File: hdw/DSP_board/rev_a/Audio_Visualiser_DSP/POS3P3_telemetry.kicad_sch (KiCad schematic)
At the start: 0 parts

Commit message: Added POS3P3 telemetry
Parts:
- added C501, C502, C503: 0.1uF, Capacitors_SMD:C_0402, symbol Custom_Library:C_Custom
- added DOC501, DOC502: TBD, symbol Custom_Library:I2C_Address
- added U501: INA231A, Custom Footprints Library:Texas_DSBGA-12_1.65x1.39mm_Layout3x4_P0.4mm, symbol Custom Library:INA231A
- added U502: MCP9804, Package_DFN_QFN:DFN-8-1EP_3x2mm_P0.5mm_EP1.3x1.5mm, symbol Sensor_Temperature:MCP9804_DFN
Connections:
- new net +3.3V: C502.1, C503.1, U501.B1 (VS), U501.D1 (BUS), U502.8 (V_{DD})
- new net GND: C502.2, C503.2, U501.C1 (GND), U502.4 (GND), U502.9 (EP/GND)
- new net I2C_SCL: U501.A1 (SCL), U502.2 (SCL)
- new net I2C_SDA: U501.A2 (SDA), U502.1 (SDA)
- new net POS3P3_SNS+: C501.1, U501.D3 (IN+)
- new net POS3P3_SNS-: C501.2, U501.D2 (IN-)
- no-connect marks 0 -> 2
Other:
- note added: "Max Current = 3.1A RSHUNT = 0.02 Ohm CLSB = 9.46045E-05A CAL Register = 0x0A92"

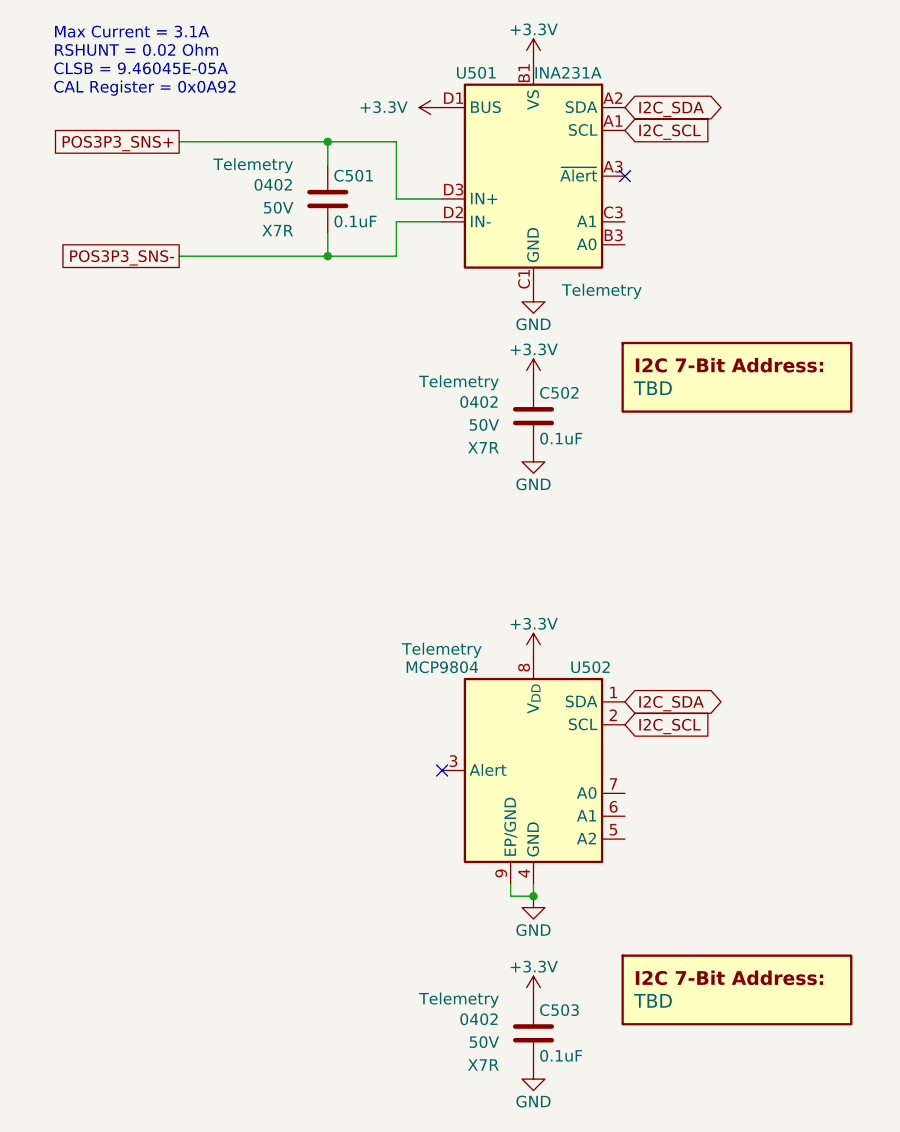
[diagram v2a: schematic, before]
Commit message: Defined legit KiCad BOM variants
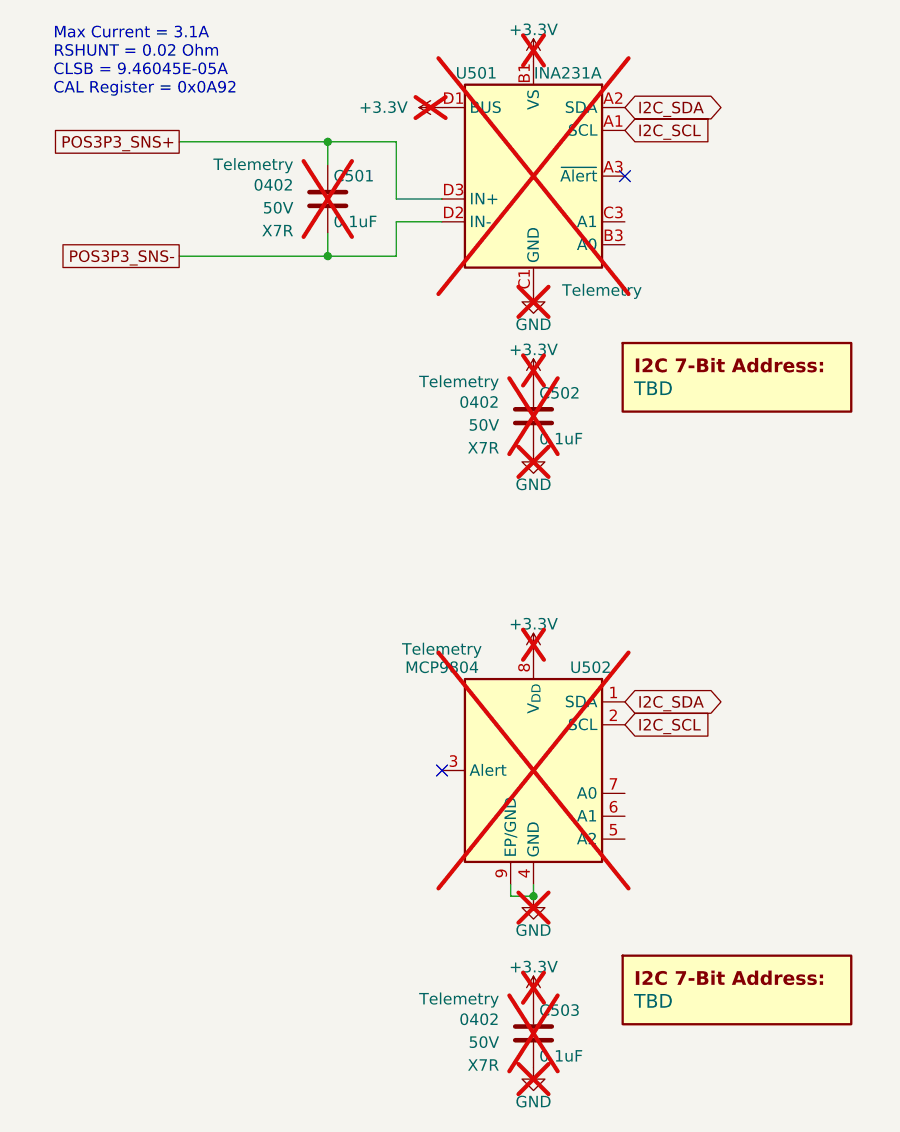
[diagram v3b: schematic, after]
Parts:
- C501, C502, C503, U501, U502: now not fitted
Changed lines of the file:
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@@
 		(on_board yes)
 		(in_pos_files yes)
-		(dnp no)
+		(dnp yes)
 		(property "Reference" "#PWR0508"
 			(at 132.08 148.59 0)
@@
 		(on_board yes)
 		(in_pos_files yes)
-		(dnp no)
+		(dnp yes)
 		(property "Reference" "#PWR0506"
 			(at 132.08 110.49 0)
@@
 		(on_board yes)
 		(in_pos_files yes)
-		(dnp no)
+		(dnp yes)
 		(property "Reference" "U501"
 			(at 125.73 41.91 0)
@@
 					(reference "U501")
 					(unit 1)
+					(variant
+						(name "Default")
+					)
+					(variant
+						(name "Development")
+						(dnp no)
+					)
 				)
 			)
@@
 		(on_board yes)
 		(in_pos_files yes)
-		(dnp no)
+		(dnp yes)
 		(fields_autoplaced yes)
 		(property "Reference" "#PWR0501"
@@
 					(reference "DOC501")
 					(unit 1)
+					(variant
+						(name "Default")
+					)
+					(variant
+						(name "Development")
+					)
 				)
 			)
@@
 		(on_board yes)
 		(in_pos_files yes)
-		(dnp no)
+		(dnp yes)
 		(property "Reference" "#PWR0503"
 			(at 132.08 72.39 0)
@@
 		(on_board yes)
 		(in_pos_files yes)
-		(dnp no)
+		(dnp yes)
 		(property "Reference" "#PWR0502"
 			(at 132.08 44.45 0)
@@
 					(reference "DOC502")
 					(unit 1)
+					(variant
+						(name "Default")
+					)
+					(variant
+						(name "Development")
+					)
 				)
 			)
@@
 		(on_board yes)
 		(in_pos_files yes)
-		(dnp no)
+		(dnp yes)
 		(property "Reference" "#PWR0505"
 			(at 132.08 90.17 0)
@@
 		(on_board yes)
 		(in_pos_files yes)
-		(dnp no)
+		(dnp yes)
 		(property "Reference" "C502"
 			(at 132.715 77.47 0)
@@
 					(reference "C502")
 					(unit 1)
+					(variant
+						(name "Default")
+					)
+					(variant
+						(name "Development")
+						(dnp no)
+					)
 				)
 			)
@@
 		(on_board yes)
 		(in_pos_files yes)
-		(dnp no)
+		(dnp yes)
 		(property "Reference" "C503"
 			(at 132.715 146.05 0)
@@
 					(reference "C503")
 					(unit 1)
+					(variant
+						(name "Default")
+					)
+					(variant
+						(name "Development")
+						(dnp no)
+					)
 				)
 			)
@@
 		(on_board yes)
 		(in_pos_files yes)
-		(dnp no)
+		(dnp yes)
 		(property "Reference" "#PWR0509"
 			(at 132.08 158.75 0)
@@
 		(on_board yes)
 		(in_pos_files yes)
-		(dnp no)
+		(dnp yes)
 		(property "Reference" "#PWR0504"
 			(at 132.08 80.01 0)
@@
 		(on_board yes)
 		(in_pos_files yes)
-		(dnp no)
+		(dnp yes)
 		(property "Reference" "#PWR0507"
 			(at 132.08 139.7 0)
@@
 		(on_board yes)
 		(in_pos_files yes)
-		(dnp no)
+		(dnp yes)
 		(property "Reference" "U502"
 			(at 138.43 107.95 0)
@@
 					(reference "U502")
 					(unit 1)
+					(variant
+						(name "Default")
+					)
+					(variant
+						(name "Development")
+						(dnp no)
+					)
 				)
 			)
@@
 		(on_board yes)
 		(in_pos_files yes)
-		(dnp no)
+		(dnp yes)
 		(property "Reference" "C501"
 			(at 109.855 53.34 0)
@@
 					(reference "C501")
 					(unit 1)
-				)
-			)
+					(variant
+						(name "Default")
+					)
+					(variant
+						(name "Development")
+						(dnp no)
+					)
+				)
+			)

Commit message: set I2C addresses
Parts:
- DOC501: value TBD -> 0x41
- DOC502: value TBD -> 0x19
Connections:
- net +3.3V: now also U501.B3 (A0), U502.7 (A0)
- net GND: now also U501.C3 (A1), U502.5 (A2), U502.6 (A1)

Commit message: Assigned I2C addresses
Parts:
- DOC501: value 0x41 -> 0x43
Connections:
- net +3.3V: no longer U501.B3 (A0)
- net I2C_SCL: now also U501.B3 (A0)
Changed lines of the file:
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@@
+		)
+	)
+	(global_label "I2C_SCL"
+		(shape input)
+		(at 142.24 60.96 0)
+		(fields_autoplaced yes)
+		(effects
+			(font
+				(size 1.27 1.27)
+			)
+			(justify left)
+		)
+		(property "Intersheetrefs" "${INTERSHEET_REFS}"
+			(at 152.7053 60.96 0)
+			(hide yes)
+			(show_name no)
+			(do_not_autoplace no)
+			(effects
+				(font
+					(size 1.27 1.27)
+				)
+				(justify left)
+			)
 		)
 	)
@@
 	)
 	(symbol
+		(lib_name "GND_1")
+		(lib_id "power:GND")
+		(at 142.24 58.42 90)
+		(unit 1)
+		(body_style 1)
+		(exclude_from_sim no)
+		(in_bom yes)
+		(on_board yes)
+		(in_pos_files yes)
+		(dnp no)
+		(fields_autoplaced yes)
+		(property "Reference" "#PWR0510"
+			(at 148.59 58.42 0)
+			(hide yes)
+			(show_name no)
+			(do_not_autoplace no)
+			(effects
+				(font
+					(size 1.27 1.27)
+				)
+			)
+		)
+		(property "Value" "GND"
+			(at 146.05 58.4199 90)
+			(show_name no)
+			(do_not_autoplace no)
+			(effects
+				(font
+					(size 1.27 1.27)
+				)
+				(justify right)
+			)
+		)
+		(property "Footprint" ""
+			(at 142.24 58.42 0)
+			(hide yes)
+			(show_name no)
+			(do_not_autoplace no)
+			(effects
+				(font
+					(size 1.27 1.27)
+				)
+			)
+		)
+		(property "Datasheet" ""
+			(at 142.24 58.42 0)
+			(hide yes)
+			(show_name no)
+			(do_not_autoplace no)
+			(effects
+				(font
+					(size 1.27 1.27)
+				)
+			)
+		)
+		(property "Description" "Power symbol creates a global label with name \"GND\" , ground"
+			(at 142.24 58.42 0)
+			(hide yes)
+			(show_name no)
+			(do_not_autoplace no)
+			(effects
+				(font
+					(size 1.27 1.27)
+				)
+			)
+		)
+		(pin "1"
+		)
+		(instances
+			(project "Audio_Visualiser_DSP"
+				(path "/97a4dfb8-0e16-46f1-9709-8d2007dd0cd3/591fe591-cb36-4c0a-afd1-91c877291a0e"
+					(reference "#PWR0510")
+					(unit 1)
+				)
+			)
+		)
+	)
+	(symbol
 		(lib_id "power:+3.3V")
 		(at 132.08 144.78 0)
@@
 			)
 		)
-		(property "Value" "0x41"
+		(property "Value" "0x43"
 			(at 143.256 76.962 0)
 			(show_name no)
@@
 						(name "Development")
 						(dnp no)
-					)
-				)
-			)
-		)
-	)
-	(symbol
-		(lib_id "power:+3.3V")
-		(at 142.24 60.96 270)
-		(unit 1)
-		(body_style 1)
-		(exclude_from_sim yes)
-		(in_bom yes)
-		(on_board yes)
-		(in_pos_files yes)
-		(dnp no)
-		(fields_autoplaced yes)
-		(property "Reference" "#PWR0514"
-			(at 138.43 60.96 0)
-			(hide yes)
-			(show_name no)
-			(do_not_autoplace no)
-			(effects
-				(font
-					(size 1.27 1.27)
-				)
-			)
-		)
-		(property "Value" "+3.3V"
-			(at 146.05 60.9599 90)
-			(show_name no)
-			(do_not_autoplace no)
-			(effects
-				(font
-					(size 1.27 1.27)
-				)
-				(justify left)
-			)
-		)
-		(property "Footprint" ""
-			(at 142.24 60.96 0)
-			(hide yes)
-			(show_name no)
-			(do_not_autoplace no)
-			(effects
-				(font
-					(size 1.27 1.27)
-				)
-			)
-		)
-		(property "Datasheet" ""
-			(at 142.24 60.96 0)
-			(hide yes)
-			(show_name no)
-			(do_not_autoplace no)
-			(effects
-				(font
-					(size 1.27 1.27)
-				)
-			)
-		)
-		(property "Description" "Power symbol creates a global label with name \"+3.3V\""
-			(at 142.24 60.96 0)
-			(hide yes)
-			(show_name no)
-			(do_not_autoplace no)
-			(effects
-				(font
-					(size 1.27 1.27)
-				)
-			)
-		)
-		(pin "1"
-		)
-		(instances
-			(project "Audio_Visualiser_DSP"
-				(path "/97a4dfb8-0e16-46f1-9709-8d2007dd0cd3/591fe591-cb36-4c0a-afd1-91c877291a0e"
-					(reference "#PWR0514")
-					(unit 1)
-					(variant
-						(name "Development")
 					)
 				)
@@
 					(unit 1)
 				)
-			)
-		)
-	)
-	(symbol
-		(lib_name "GND_1")
-		(lib_id "power:GND")
-		(at 142.24 58.42 90)
-		(unit 1)
-		(body_style 1)
-		(exclude_from_sim no)
-		(in_bom yes)
-		(on_board yes)
-		(in_pos_files yes)
-		(dnp no)
-		(fields_autoplaced yes)
-		(property "Reference" "#PWR0510"
-			(at 148.59 58.42 0)
-			(hide yes)
-			(show_name no)
-			(do_not_autoplace no)
-			(effects
-				(font
-					(size 1.27 1.27)
-				)
-			)
-		)
-		(property "Value" "GND"
-			(at 146.05 58.4199 90)
-			(show_name no)
-			(do_not_autoplace no)
-			(effects
-				(font
-					(size 1.27 1.27)
-				)
-				(justify right)
-			)
-		)
-		(property "Footprint" ""
-			(at 142.24 58.42 0)
-			(hide yes)
-			(show_name no)
-			(do_not_autoplace no)
-			(effects
-				(font
-					(size 1.27 1.27)
-				)
-			)
-		)
-		(property "Datasheet" ""
-			(at 142.24 58.42 0)
-			(hide yes)
-			(show_name no)
-			(do_not_autoplace no)
-			(effects
-				(font
-					(size 1.27 1.27)
-				)
-			)
-		)
-		(property "Description" "Power symbol creates a global label with name \"GND\" , ground"
-			(at 142.24 58.42 0)
-			(hide yes)
-			(show_name no)
-			(do_not_autoplace no)
-			(effects
-				(font
-					(size 1.27 1.27)
-				)
-			)
-		)
-		(pin "1"
-		)
-		(instances
-			(project "Audio_Visualiser_DSP"
-				(path "/97a4dfb8-0e16-46f1-9709-8d2007dd0cd3/591fe591-cb36-4c0a-afd1-91c877291a0e"
-					(reference "#PWR0510")
-					(unit 1)
-				)

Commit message: Consolidated onto a single project library
This commit combines all schematic symbols, pcb footprints, and 3d models into a single project library for portability. Still have a few 3d models to add yet. It also removes each individual custom component which had been stored in this repo earlier
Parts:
- C501, C502, C503: footprint Capacitors_SMD:C_0402 -> project_lib:C_0402; symbol Custom_Library:C_Custom -> project_lib:C_Custom
- DOC501, DOC502: symbol Custom_Library:I2C_Address -> project_lib:I2C_Address
- U501: footprint Custom Footprints Library:Texas_DSBGA-12_1.65x1.39mm_Layout3x4_P0.4mm -> project_lib:Texas_DSBGA-12_1.65x1.39mm_Layout3x4_P0.4mm; symbol Custom Library:INA231A -> project_lib:INA231A
- U502: footprint Package_DFN_QFN:DFN-8-1EP_3x2mm_P0.5mm_EP1.3x1.5mm -> project_lib:DFN-8-1EP_3x2mm_P0.5mm_EP1.3x1.5mm; symbol Sensor_Temperature:MCP9804_DFN -> project_lib:MCP9804_DFN
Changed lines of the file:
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@@
 	)
 	(symbol
-		(lib_name "GND_1")
-		(lib_id "power:GND")
+		(lib_id "project_lib:GND")
 		(at 142.24 58.42 90)
 		(unit 1)
@@
 	)
 	(symbol
-		(lib_id "power:+3.3V")
+		(lib_id "project_lib:+3.3V")
 		(at 132.08 144.78 0)
 		(unit 1)
@@
 	)
 	(symbol
-		(lib_id "power:+3.3V")
+		(lib_id "project_lib:+3.3V")
 		(at 132.08 106.68 0)
 		(unit 1)
@@
 	)
 	(symbol
-		(lib_id "Custom Library:INA231A")
+		(lib_id "project_lib:INA231A")
 		(at 132.08 53.34 0)
 		(unit 1)
@@
 			)
 		)
-		(property "Footprint" "Custom Footprints Library:Texas_DSBGA-12_1.65x1.39mm_Layout3x4_P0.4mm"
+		(property "Footprint" "project_lib:Texas_DSBGA-12_1.65x1.39mm_Layout3x4_P0.4mm"
 			(at 152.4 64.77 0)
 			(hide yes)
@@
 	)
 	(symbol
-		(lib_id "power:+3.3V")
+		(lib_id "project_lib:+3.3V")
 		(at 121.92 45.72 90)
 		(unit 1)
@@
 	)
 	(symbol
-		(lib_id "Custom_Library:I2C_Address")
+		(lib_id "project_lib:I2C_Address")
 		(at 154.686 76.962 0)
 		(unit 1)
@@
 	)
 	(symbol
-		(lib_id "power:GND")
+		(lib_id "project_lib:GND")
 		(at 132.08 66.04 0)
 		(unit 1)
@@
 	)
 	(symbol
-		(lib_id "power:+3.3V")
+		(lib_id "project_lib:+3.3V")
 		(at 132.08 40.64 0)
 		(unit 1)
@@
 	)
 	(symbol
-		(lib_id "Custom_Library:I2C_Address")
+		(lib_id "project_lib:I2C_Address")
 		(at 154.686 145.034 0)
 		(unit 1)
@@
 	)
 	(symbol
-		(lib_id "power:GND")
+		(lib_id "project_lib:GND")
 		(at 132.08 83.82 0)
 		(unit 1)
@@
 	)
 	(symbol
-		(lib_name "GND_1")
-		(lib_id "power:GND")
+		(lib_id "project_lib:GND")
 		(at 142.24 124.46 90)
 		(unit 1)
@@
 	)
 	(symbol
-		(lib_id "Custom_Library:C_Custom")
+		(lib_id "project_lib:C_Custom")
 		(at 132.08 80.01 0)
 		(unit 1)
@@
 			)
 		)
-		(property "Footprint" "Capacitors_SMD:C_0402"
+		(property "Footprint" "project_lib:C_0402"
 			(at 133.0452 83.82 0)
 			(hide yes)
@@
 	)
 	(symbol
-		(lib_id "power:+3.3V")
+		(lib_id "project_lib:+3.3V")
 		(at 142.24 121.92 270)
 		(unit 1)
@@
 	)
 	(symbol
-		(lib_id "Custom_Library:C_Custom")
+		(lib_id "project_lib:C_Custom")
 		(at 132.08 148.59 0)
 		(unit 1)
@@
 			)
 		)
-		(property "Footprint" "Capacitors_SMD:C_0402"
+		(property "Footprint" "project_lib:C_0402"
 			(at 133.0452 152.4 0)
 			(hide yes)
@@
 	)
 	(symbol
-		(lib_id "power:GND")
+		(lib_id "project_lib:GND")
 		(at 132.08 152.4 0)
 		(unit 1)
@@
 	)
 	(symbol
-		(lib_name "GND_1")
-		(lib_id "power:GND")
+		(lib_id "project_lib:GND")
 		(at 142.24 127 90)
 		(unit 1)
@@
 	)
 	(symbol
-		(lib_id "power:+3.3V")
+		(lib_id "project_lib:+3.3V")
 		(at 132.08 76.2 0)
 		(unit 1)
@@
 	)
 	(symbol
-		(lib_id "power:GND")
+		(lib_id "project_lib:GND")
 		(at 132.08 133.35 0)
 		(mirror y)
@@
 	)
 	(symbol
-		(lib_id "Sensor_Temperature:MCP9804_DFN")
+		(lib_id "project_lib:MCP9804_DFN")
 		(at 132.08 119.38 0)
 		(mirror y)
@@
 			)
 		)
-		(property "Footprint" "Package_DFN_QFN:DFN-8-1EP_3x2mm_P0.5mm_EP1.3x1.5mm"
+		(property "Footprint" "project_lib:DFN-8-1EP_3x2mm_P0.5mm_EP1.3x1.5mm"
 			(at 160.02 132.08 0)
 			(hide yes)
@@
 	)
 	(symbol
-		(lib_id "Custom_Library:C_Custom")
+		(lib_id "project_lib:C_Custom")
 		(at 109.22 55.88 0)
 		(unit 1)
@@
 			)
 		)
-		(property "Footprint" "Capacitors_SMD:C_0402"
+		(property "Footprint" "project_lib:C_0402"
 			(at 110.1852 59.69 0)
 			(hide yes)
